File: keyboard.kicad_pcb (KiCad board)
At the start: 2 copper layers, 12 x 21 mm, 68 parts, among them J1 Conn_01x04_Socket, J3 Conn_01x02_Socket, SW1 SW_Push, SW10 SW_Push, SW11 SW_Push, SW12 SW_Push, SW13 SW_Push, SW14 SW_Push, SW15 SW_Push, SW16 SW_Push, SW17 SW_Push, SW18 SW_Push, SW19 SW_Push, SW2 SW_Push, SW20 SW_Push, SW21 SW_Push, SW22 SW_Push, SW23 SW_Push, SW24 SW_Push, SW25 SW_Push, SW26 SW_Push, SW27 SW_Push, SW28 SW_Push, SW3 SW_Push, SW4 SW_Push, SW401 SW_Push, SW402 SW_Push, SW5 SW_Push, SW6 SW_Push, SW7 SW_Push, SW8 SW_Push, SW9 SW_Push, U1 rp2040-zero

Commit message: なんとなく形になったので一旦commit
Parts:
- J1: value Conn_01x04_Socket -> Conn_01x06_Socket; footprint Connector_PinHeader_2.54mm:PinHeader_1x04_P2.54mm_Vertical -> Connector_PinHeader_2.54mm:PinHeader_1x06_P2.54mm_Vertical
- SW5: renamed from SW401; footprint kbd:keyswitch_cherrymx_hotswap_2u -> kbd:keyswitch_cherrymx_hotswap_1u
- moved SW5 115.0 mm to (76.2, 134.0)
- moved U1 112.0 mm to (204.5, 56.5)
- moved D26 110.1 mm to (171.4, 61.6)
- moved D25 101.5 mm to (212.6, 132.3), turned to -15 degrees
- moved D16 99.8 mm to (133.3, 55.2)
- moved JC1 95.3 mm to (186.3, 57.1)
- moved D30 89.6 mm to (208.1, 150.5), turned to -15 degrees
- moved D21 87.1 mm to (152.4, 60.3)
- moved D17 84.8 mm to (133.3, 74.3)
- moved D6 82.1 mm to (95.2, 62.9)
- moved JP1 79.8 mm to (189.2, 74.8)
- moved J1 78.2 mm to (204.5, 72.4)
- moved D11 77.1 mm to (114.3, 57.8)
- moved R1 74.2 mm to (189.2, 63.4)
- moved R2 74.2 mm to (189.2, 66.7)
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- renumbered D9 to D10, D10 to D11, D11 to D12, D12 to D13, D13 to D14, D14 to D15, D15 to D16, D16 to D17, D17 to D18, D18 to D19, D402 to D20, D19 to D21, D20 to D22, D21 to D23, D22 to D24, D23 to D25, D24 to D26, D25 to D27, D26 to D28, D27 to D29, D28 to D30, D401 to D5, D5 to D6, D6 to D7, D7 to D8, D8 to D9, SW9 to SW10, SW10 to SW11, SW11 to SW12, SW12 to SW13, SW13 to SW14, SW14 to SW15, SW15 to SW16, SW16 to SW17, SW17 to SW18, SW18 to SW19, SW402 to SW20, SW19 to SW21, SW20 to SW22, SW21 to SW23, SW22 to SW24, SW23 to SW25, SW24 to SW26, SW25 to SW27, SW26 to SW28, SW27 to SW29, SW28 to SW30, SW5 to SW6, SW6 to SW7, SW7 to SW8, SW8 to SW9
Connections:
- JC1 pad S: Net-(U1-15) -> Net-(J1-Pin_5)
- JC1 pad T: Net-(JP1-A) -> Net-(J1-Pin_6)
- JP1 pad 1: Net-(JP1-A) -> Net-(J1-Pin_6)
- R1 pad 1: Net-(JP1-A) -> Net-(J1-Pin_6)
- R2 pad 1: Net-(JP1-A) -> Net-(J1-Pin_6)
- R5 pad 2: Net-(U1-15) -> Net-(J1-Pin_5)
- U1 pad 16: Net-(U1-15) -> Net-(J1-Pin_5)
- U1 pad 22: Net-(U1-15) -> Net-(J1-Pin_5)
- U1 pad 23: Net-(JP1-A) -> Net-(J1-Pin_6)

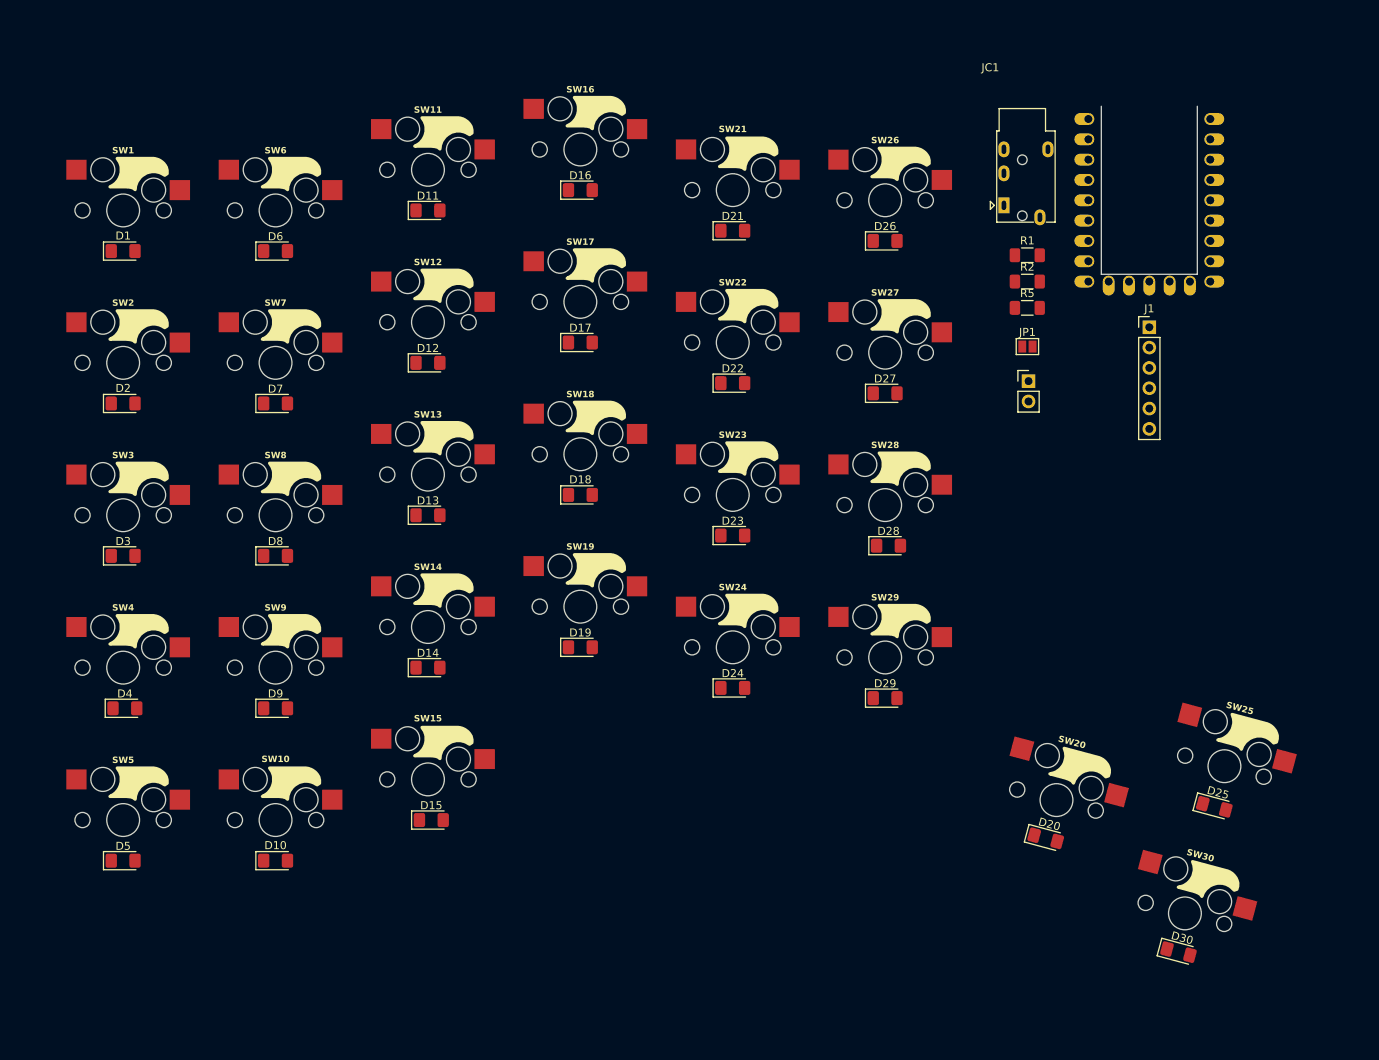
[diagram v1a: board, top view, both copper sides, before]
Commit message: キースイッチとダイオードを基板裏側に移動
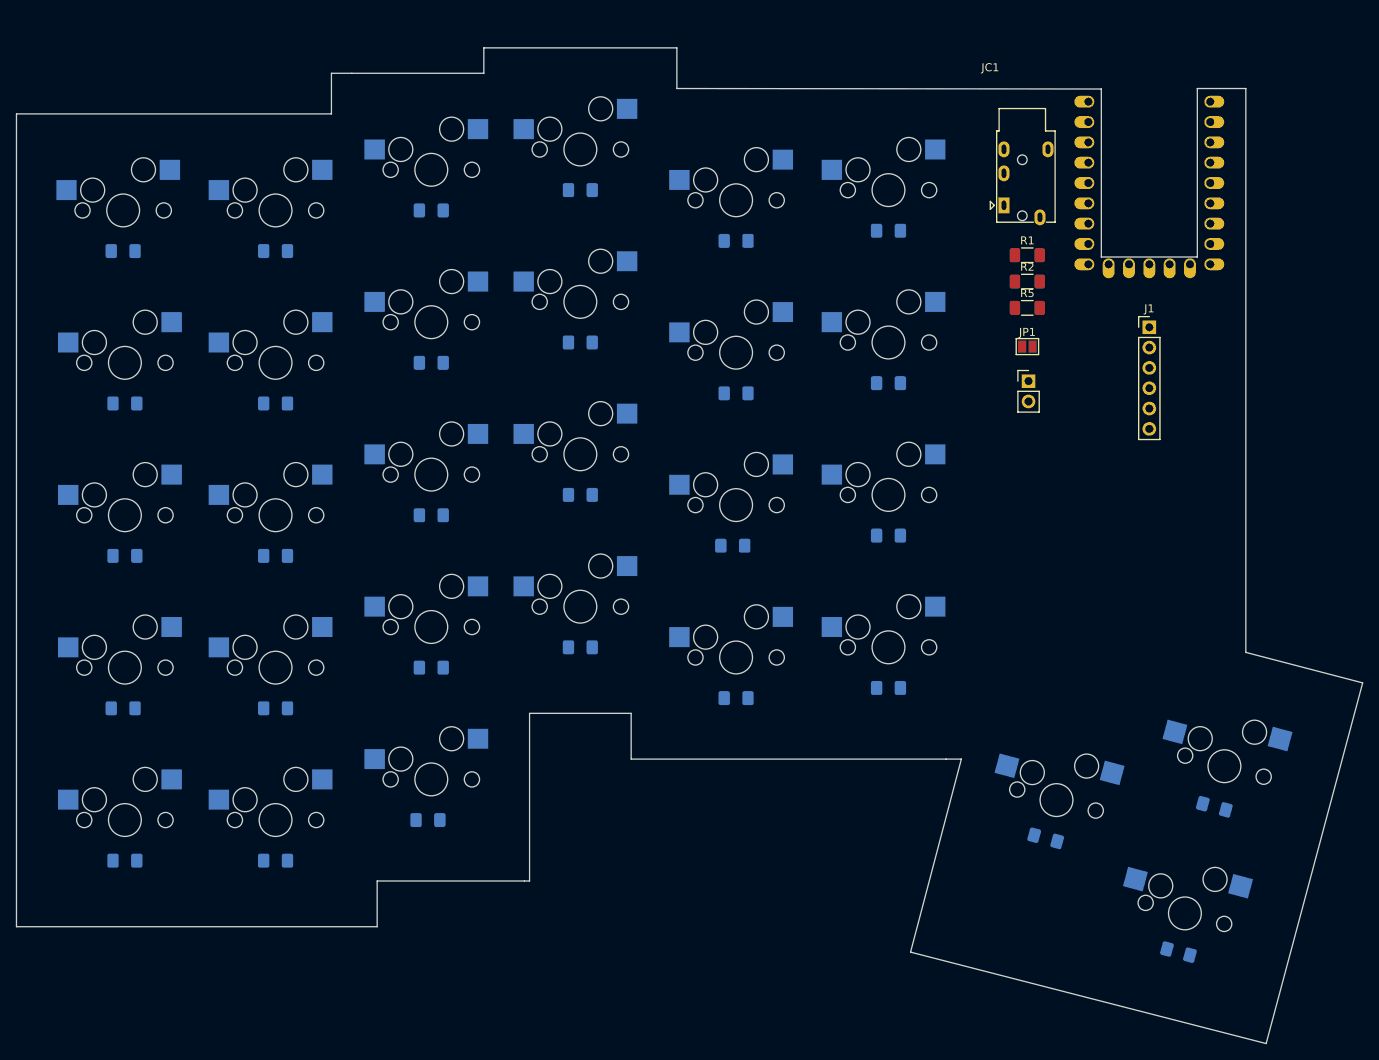
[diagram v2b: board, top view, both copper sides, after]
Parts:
- D1, D10, D11, D12, D13, D14, D15, D16, D17, D18, D19, D2, D20, D21, D22, D23, D24, D25, D26, D27, D28, D29, D3, D30, D4, D5, D6, D7, D8, D9, SW1, SW10, SW11, SW12, SW13, SW14, SW15, SW16, SW17, SW18, SW19, SW2, SW20, SW21, SW22, SW23, SW24, SW25, SW26, SW27, SW28, SW29, SW3, SW30, SW4, SW5, SW6, SW7, SW8, SW9, U1: moved to B.Cu
- moved D21 19.5 mm to (171.9, 60.3), turned to 180 degrees
- moved D22 19.5 mm to (171.9, 79.4), turned to 180 degrees
- moved D23 19.5 mm to (171.9, 98.4), turned to 180 degrees
- moved D24 19.5 mm to (171.9, 117.5), turned to 180 degrees
- moved D28 19.5 mm to (152.4, 99.7), turned to 180 degrees
- moved SW21 19.5 mm to (171.9, 55.2), turned to 180 degrees
- moved SW22 19.5 mm to (171.9, 74.3), turned to 180 degrees
- moved SW23 19.5 mm to (171.9, 93.3), turned to 180 degrees
- moved SW24 19.5 mm to (171.9, 112.4), turned to 180 degrees
- moved D26 18.6 mm to (152.8, 61.6), turned to 180 degrees
- moved D27 18.6 mm to (152.8, 80.6), turned to 180 degrees
- moved D29 18.6 mm to (152.8, 118.7), turned to 180 degrees
- moved SW26 18.6 mm to (152.8, 56.5), turned to 180 degrees
- moved SW27 18.6 mm to (152.8, 75.6), turned to 180 degrees
- moved SW28 18.6 mm to (152.8, 94.6), turned to 180 degrees
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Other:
- board size 12 x 21 mm -> 168.3 x 124.5 mm

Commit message: 一旦保存2
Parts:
- moved JC1 19.6 mm to (205.1, 51.7)
- moved U1 12.1 mm to (192.4, 54.2)
- moved JP1 8.37 mm to (196.1, 70.0)
- moved J3 8.37 mm to (196.2, 74.3)
- moved R2 7.04 mm to (187.7, 73.5)
- moved R1 7.04 mm to (187.7, 70.3)
- moved R5 7.04 mm to (187.7, 76.8)
- moved D23 4.45 mm to (171.9, 102.9)
- moved D24 4.45 mm to (171.9, 121.9)
- moved SW23 4.45 mm to (171.9, 97.8)
- moved SW24 4.45 mm to (171.9, 116.8)
- moved SW21 4.45 mm to (171.9, 59.7)
- moved D21 4.44 mm to (171.9, 64.8)
- moved D22 4.44 mm to (171.9, 83.8)
- moved SW22 4.44 mm to (171.9, 78.7)
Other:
- outline, holes or cut-outs redrawn

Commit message: pcb大体並べたので一旦保存
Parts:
- added D31: D, Diode_SMD:D_1206_3216Metric_Pad1.42x1.75mm_HandSolder, F.Cu at (76.3, 49.5)
- added D32: D, Diode_SMD:D_1206_3216Metric_Pad1.42x1.75mm_HandSolder, F.Cu at (76.2, 68.6)
- added D33: D, Diode_SMD:D_1206_3216Metric_Pad1.42x1.75mm_HandSolder, F.Cu at (76.2, 87.6)
- added D34: D, Diode_SMD:D_1206_3216Metric_Pad1.42x1.75mm_HandSolder, F.Cu at (76.0, 106.7)
- added D35: D, Diode_SMD:D_1206_3216Metric_Pad1.42x1.75mm_HandSolder, F.Cu at (76.2, 125.7)
- added D36: D, Diode_SMD:D_1206_3216Metric_Pad1.42x1.75mm_HandSolder, F.Cu at (95.5, 49.5)
- added D37: D, Diode_SMD:D_1206_3216Metric_Pad1.42x1.75mm_HandSolder, F.Cu at (95.0, 68.6)
- added D38: D, Diode_SMD:D_1206_3216Metric_Pad1.42x1.75mm_HandSolder, F.Cu at (95.0, 87.6)
- added D39: D, Diode_SMD:D_1206_3216Metric_Pad1.42x1.75mm_HandSolder, F.Cu at (95.0, 106.7)
- added D40: D, Diode_SMD:D_1206_3216Metric_Pad1.42x1.75mm_HandSolder, F.Cu at (95.2, 125.7)
- added D41: D, Diode_SMD:D_1206_3216Metric_Pad1.42x1.75mm_HandSolder, F.Cu at (114.3, 44.5)
- added D42: D, Diode_SMD:D_1206_3216Metric_Pad1.42x1.75mm_HandSolder, F.Cu at (114.1, 63.5)
- added D43: D, Diode_SMD:D_1206_3216Metric_Pad1.42x1.75mm_HandSolder, F.Cu at (114.3, 82.5)
- added D44: D, Diode_SMD:D_1206_3216Metric_Pad1.42x1.75mm_HandSolder, F.Cu at (114.5, 101.6)
- added D45: D, Diode_SMD:D_1206_3216Metric_Pad1.42x1.75mm_HandSolder, F.Cu at (114.5, 120.7)
- added D46: D, Diode_SMD:D_1206_3216Metric_Pad1.42x1.75mm_HandSolder, F.Cu at (133.6, 41.9)
- added D47: D, Diode_SMD:D_1206_3216Metric_Pad1.42x1.75mm_HandSolder, F.Cu at (133.1, 61.0)
- added D48: D, Diode_SMD:D_1206_3216Metric_Pad1.42x1.75mm_HandSolder, F.Cu at (133.3, 80.0)
- added D49: D, Diode_SMD:D_1206_3216Metric_Pad1.42x1.75mm_HandSolder, F.Cu at (133.3, 99.1)
- added D50: D, Diode_SMD:D_1206_3216Metric_Pad1.42x1.75mm_HandSolder, F.Cu at (195.4, 120.3)
- added D51: D, Diode_SMD:D_1206_3216Metric_Pad1.42x1.75mm_HandSolder, F.Cu at (152.2, 48.3)
- added D52: D, Diode_SMD:D_1206_3216Metric_Pad1.42x1.75mm_HandSolder, F.Cu at (152.8, 67.3)
- added D53: D, Diode_SMD:D_1206_3216Metric_Pad1.42x1.75mm_HandSolder, F.Cu at (152.6, 86.4)
- added D54: D, Diode_SMD:D_1206_3216Metric_Pad1.42x1.75mm_HandSolder, F.Cu at (152.8, 105.4)
- added D55: D, Diode_SMD:D_1206_3216Metric_Pad1.42x1.75mm_HandSolder, F.Cu at (216.1, 119.2)
- added D56: D, Diode_SMD:D_1206_3216Metric_Pad1.42x1.75mm_HandSolder, F.Cu at (171.6, 51.4)
- added D57: D, Diode_SMD:D_1206_3216Metric_Pad1.42x1.75mm_HandSolder, F.Cu at (171.5, 70.4)
- added D58: D, Diode_SMD:D_1206_3216Metric_Pad1.42x1.75mm_HandSolder, F.Cu at (171.7, 89.5)
- added D59: D, Diode_SMD:D_1206_3216Metric_Pad1.42x1.75mm_HandSolder, F.Cu at (171.3, 108.5)
- added D60: D, Diode_SMD:D_1206_3216Metric_Pad1.42x1.75mm_HandSolder, F.Cu at (210.7, 137.6)
- added J2: Conn_01x02_Socket, Connector_PinHeader_2.54mm:PinHeader_1x02_P2.54mm_Vertical, B.Cu at (196.2, 74.3)
- added J4: Conn_01x06_Socket, Connector_PinHeader_2.54mm:PinHeader_1x06_P2.54mm_Vertical, B.Cu at (208.3, 69.8)
- added JC2: AudioJack4, Connector_Audio:Jack_3.5mm_PJ320E_Horizontal, F.Cu at (207.8, 51.8)
- added JP2: Jumper_2_Open, Jumper:SolderJumper-2_P1.3mm_Open_Pad1.0x1.5mm, F.Cu at (196.2, 70.2)
- added R4: R, Resistor_SMD:R_1206_3216Metric_Pad1.30x1.75mm_HandSolder, F.Cu at (187.7, 70.2)
- added R5: R, Resistor_SMD:R_1206_3216Metric_Pad1.30x1.75mm_HandSolder, F.Cu at (187.7, 73.5)
- added R6: R, Resistor_SMD:R_1206_3216Metric_Pad1.30x1.75mm_HandSolder, F.Cu at (187.7, 76.8)
- added SW31: SW_Push, kbd:keyswitch_cherrymx_hotswap_1u, F.Cu at (76.2, 57.8)
- added SW32: SW_Push, kbd:keyswitch_cherrymx_hotswap_1u, F.Cu at (76.2, 76.8)
- added SW33: SW_Push, kbd:keyswitch_cherrymx_hotswap_1u, F.Cu at (76.2, 95.9)
- added SW34: SW_Push, kbd:keyswitch_cherrymx_hotswap_1u, F.Cu at (76.2, 114.9)
- added SW35: SW_Push, kbd:keyswitch_cherrymx_hotswap_1u, F.Cu at (76.2, 134.0)
- added SW36: SW_Push, kbd:keyswitch_cherrymx_hotswap_1u, F.Cu at (95.2, 57.8)
- added SW37: SW_Push, kbd:keyswitch_cherrymx_hotswap_1u, F.Cu at (95.2, 76.8)
- added SW38: SW_Push, kbd:keyswitch_cherrymx_hotswap_1u, F.Cu at (95.2, 95.9)
- added SW39: SW_Push, kbd:keyswitch_cherrymx_hotswap_1u, F.Cu at (95.2, 114.9)
- added SW40: SW_Push, kbd:keyswitch_cherrymx_hotswap_1u, F.Cu at (95.2, 134.0)
- added SW41: SW_Push, kbd:keyswitch_cherrymx_hotswap_1u, F.Cu at (114.3, 52.7)
- added SW42: SW_Push, kbd:keyswitch_cherrymx_hotswap_1u, F.Cu at (114.3, 71.8)
- added SW43: SW_Push, kbd:keyswitch_cherrymx_hotswap_1u, F.Cu at (114.3, 90.8)
- added SW44: SW_Push, kbd:keyswitch_cherrymx_hotswap_1u, F.Cu at (114.3, 109.9)
- added SW45: SW_Push, kbd:keyswitch_cherrymx_hotswap_1u, F.Cu at (114.3, 128.9)
- added SW46: SW_Push, kbd:keyswitch_cherrymx_hotswap_1u, F.Cu at (133.3, 50.2)
- added SW47: SW_Push, kbd:keyswitch_cherrymx_hotswap_1u, F.Cu at (133.3, 69.2)
- added SW48: SW_Push, kbd:keyswitch_cherrymx_hotswap_1u, F.Cu at (133.3, 88.3)
- added SW49: SW_Push, kbd:keyswitch_cherrymx_hotswap_1u, F.Cu at (133.3, 107.3)
- added SW50: SW_Push, kbd:keyswitch_cherrymx_hotswap_2u_vertical, F.Cu at (192.9, 131.5)
- added SW51: SW_Push, kbd:keyswitch_cherrymx_hotswap_1u, F.Cu at (152.4, 56.5)
- added SW52: SW_Push, kbd:keyswitch_cherrymx_hotswap_1u, F.Cu at (152.4, 75.6)
- added SW53: SW_Push, kbd:keyswitch_cherrymx_hotswap_1u, F.Cu at (152.4, 94.6)
- added SW54: SW_Push, kbd:keyswitch_cherrymx_hotswap_1u, F.Cu at (152.4, 113.7)
- added SW55: SW_Push, kbd:keyswitch_cherrymx_hotswap_1u, F.Cu at (208.9, 145.7)
- added SW56: SW_Push, kbd:keyswitch_cherrymx_hotswap_1u, F.Cu at (171.4, 59.7)
- added SW57: SW_Push, kbd:keyswitch_cherrymx_hotswap_1u, F.Cu at (171.4, 78.7)
- added SW58: SW_Push, kbd:keyswitch_cherrymx_hotswap_1u, F.Cu at (171.4, 97.8)
- added SW59: SW_Push, kbd:keyswitch_cherrymx_hotswap_1u, F.Cu at (171.4, 116.8)
- added SW60: SW_Push, kbd:keyswitch_cherrymx_hotswap_1u, F.Cu at (213.9, 127.3)
- added U2: rp2040-zero, mcu:rp2040-zero-tht, F.Cu at (192.4, 54.2)
- JC1, JP1, R1, R2: moved to B.Cu
- R3: renamed from R5; moved to B.Cu
- moved D29 20.1 mm to (171.9, 125.1)
- moved D27 19.9 mm to (171.7, 87.0)
- moved D28 19.9 mm to (171.2, 106.0)
- moved SW23 19.7 mm to (152.4, 94.6)
- moved SW21 19.7 mm to (152.4, 56.5)
- moved SW22 19.7 mm to (152.4, 75.6)
- moved SW24 19.7 mm to (152.4, 113.7)
- moved D26 19.7 mm to (171.4, 67.9)
- moved D21 19.2 mm to (152.6, 64.8)
- moved D22 19.2 mm to (152.6, 83.8)
- moved D23 19.2 mm to (152.6, 102.9)
- moved D24 19.2 mm to (152.6, 121.9)
- moved SW28 18.9 mm to (171.4, 97.8)
- moved SW26 18.9 mm to (171.4, 59.7)
- moved SW27 18.9 mm to (171.4, 78.7)
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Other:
- outline, holes or cut-outs redrawn

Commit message: wip
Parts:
- removed U2: rp2040-zero, mcu:rp2040-zero-tht
- moved SW60 19.1 mm to (208.8, 145.6)
- moved SW55 19.0 mm to (213.7, 127.2)
- moved JC2 18.4 mm to (206.6, 70.1), turned to -90 degrees
- moved J1 14.3 mm to (211.3, 83.8)
- moved J4 14.0 mm to (208.6, 83.8)
- moved J2 4.13 mm to (192.1, 74.6)
- moved JP1 2.30 mm to (193.9, 70.3)
- moved R1 2.30 mm to (185.4, 70.3)
- moved R2 2.30 mm to (185.4, 73.6)
- moved R3 2.30 mm to (185.4, 76.9)
- moved R4 2.30 mm to (185.4, 70.3)
- moved R5 2.30 mm to (185.4, 73.6)
- moved R6 2.30 mm to (185.4, 76.8)
- moved JP2 2.30 mm to (193.9, 70.3)
- moved J3 0.61 mm to (195.7, 74.6)
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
